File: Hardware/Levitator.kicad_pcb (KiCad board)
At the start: 2 copper layers, 54 x 46.5 mm, 9 parts, among them J1 Screw_Terminal_01x08, Q1 AOD4184A, U1 LM358

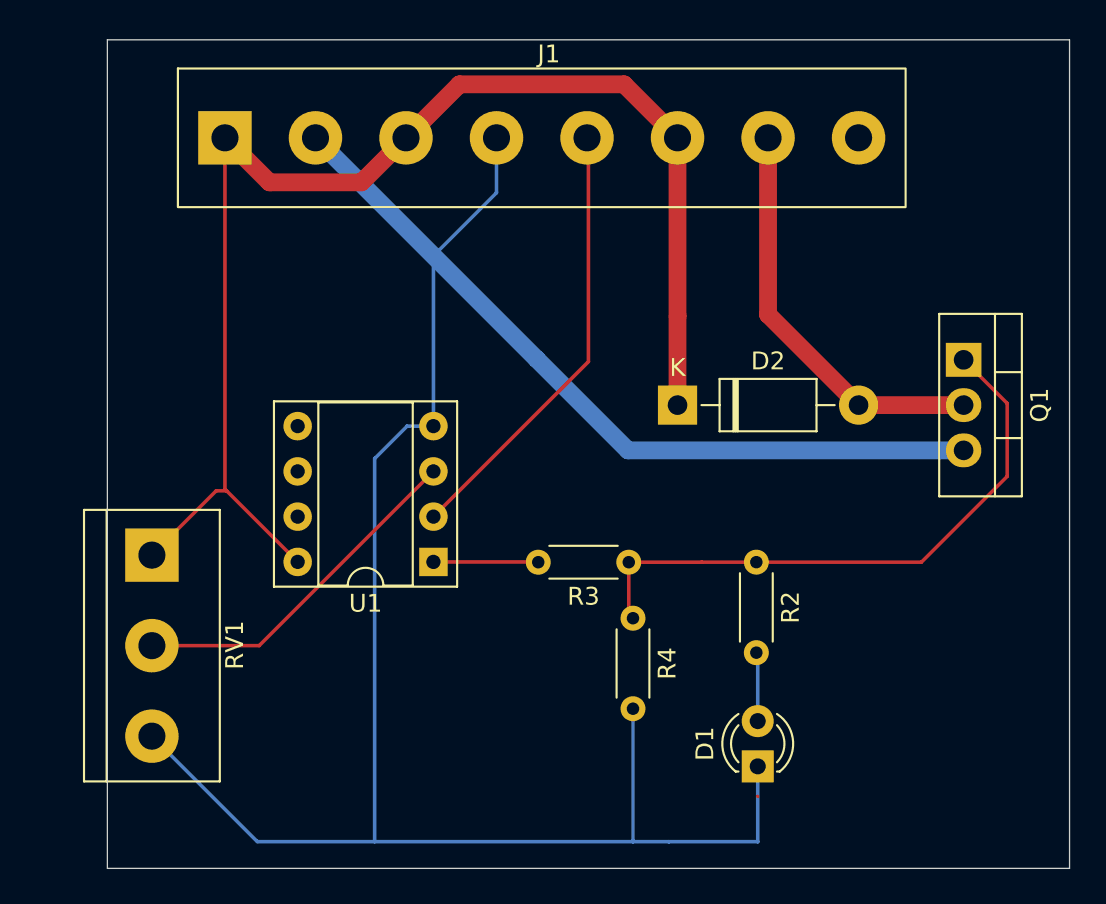
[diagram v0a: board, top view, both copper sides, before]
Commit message: feat: Moved power in to barrel socket
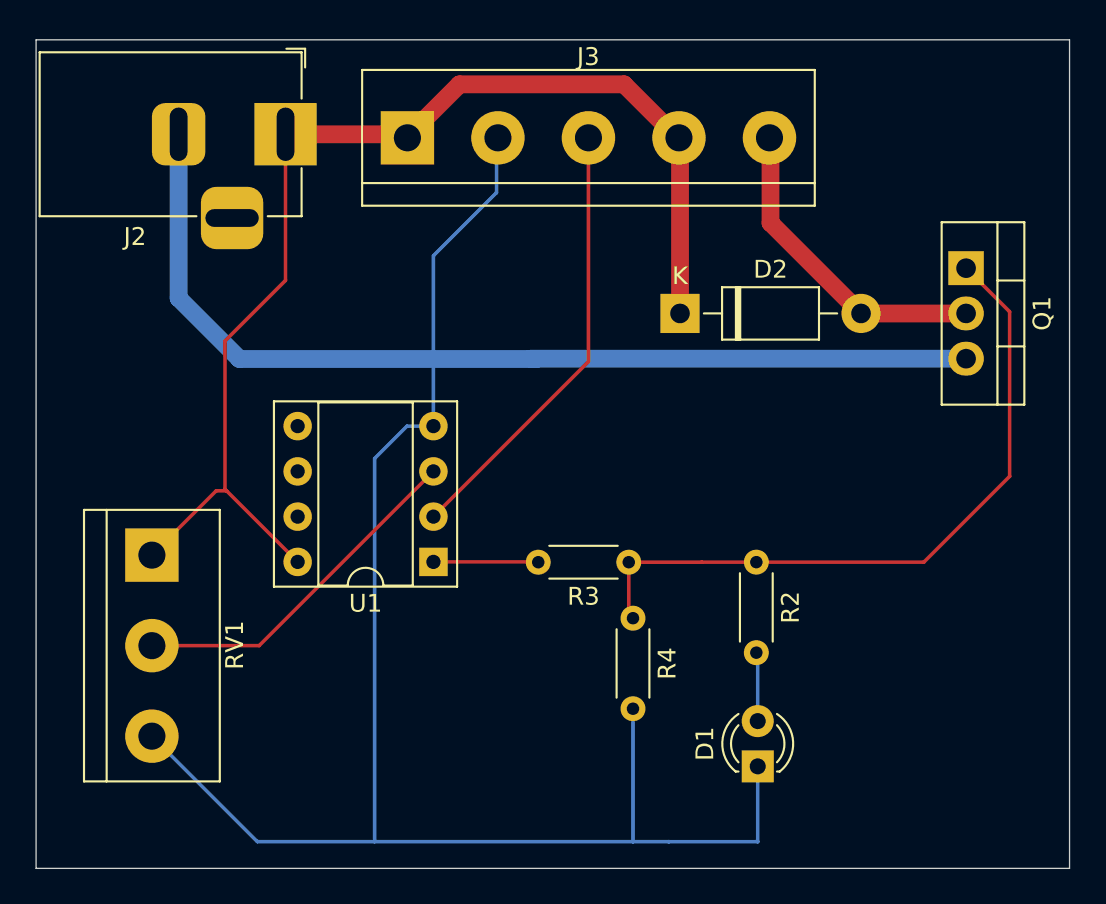
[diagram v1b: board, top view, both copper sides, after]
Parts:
- removed J1: Screw_Terminal_01x08, TerminalBlock:TerminalBlock_bornier-8_P5.08mm
- added J2: Barrel_Jack, Connector_BarrelJack:BarrelJack_Horizontal, F.Cu at (31.5, 58.8)
- added J3: Screw_Terminal_01x05, TerminalBlock:TerminalBlock_bornier-5_P5.08mm, F.Cu at (38.3, 59.0)
- moved D2 5.15 mm to (53.6, 68.9)
- moved Q1 5.15 mm to (69.7, 66.3)
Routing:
- net VCC: track 76.2 -> 67.1 mm
- net Net-(Q1-G): track 34.0 -> 39.3 mm
- net /COIL-: track 23.3 -> 18.2 mm
- net GND: track 144.3 -> 146.5 mm
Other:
- board size 54 x 46.5 mm -> 58 x 46.5 mm
